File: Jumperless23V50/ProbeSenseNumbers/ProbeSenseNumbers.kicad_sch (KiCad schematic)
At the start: 117 parts, among them J1 Conn_01x05, J2 TopOutMAIN, J3 TopIn, J31 + - top, J32 + - bottom, J33 TopInMAIN, J34 TopOut, J35 BottomIn, J36 BottomOutMAIN, J4 BottomOut, J5 BottomInMAIN, J6 Conn_01x02

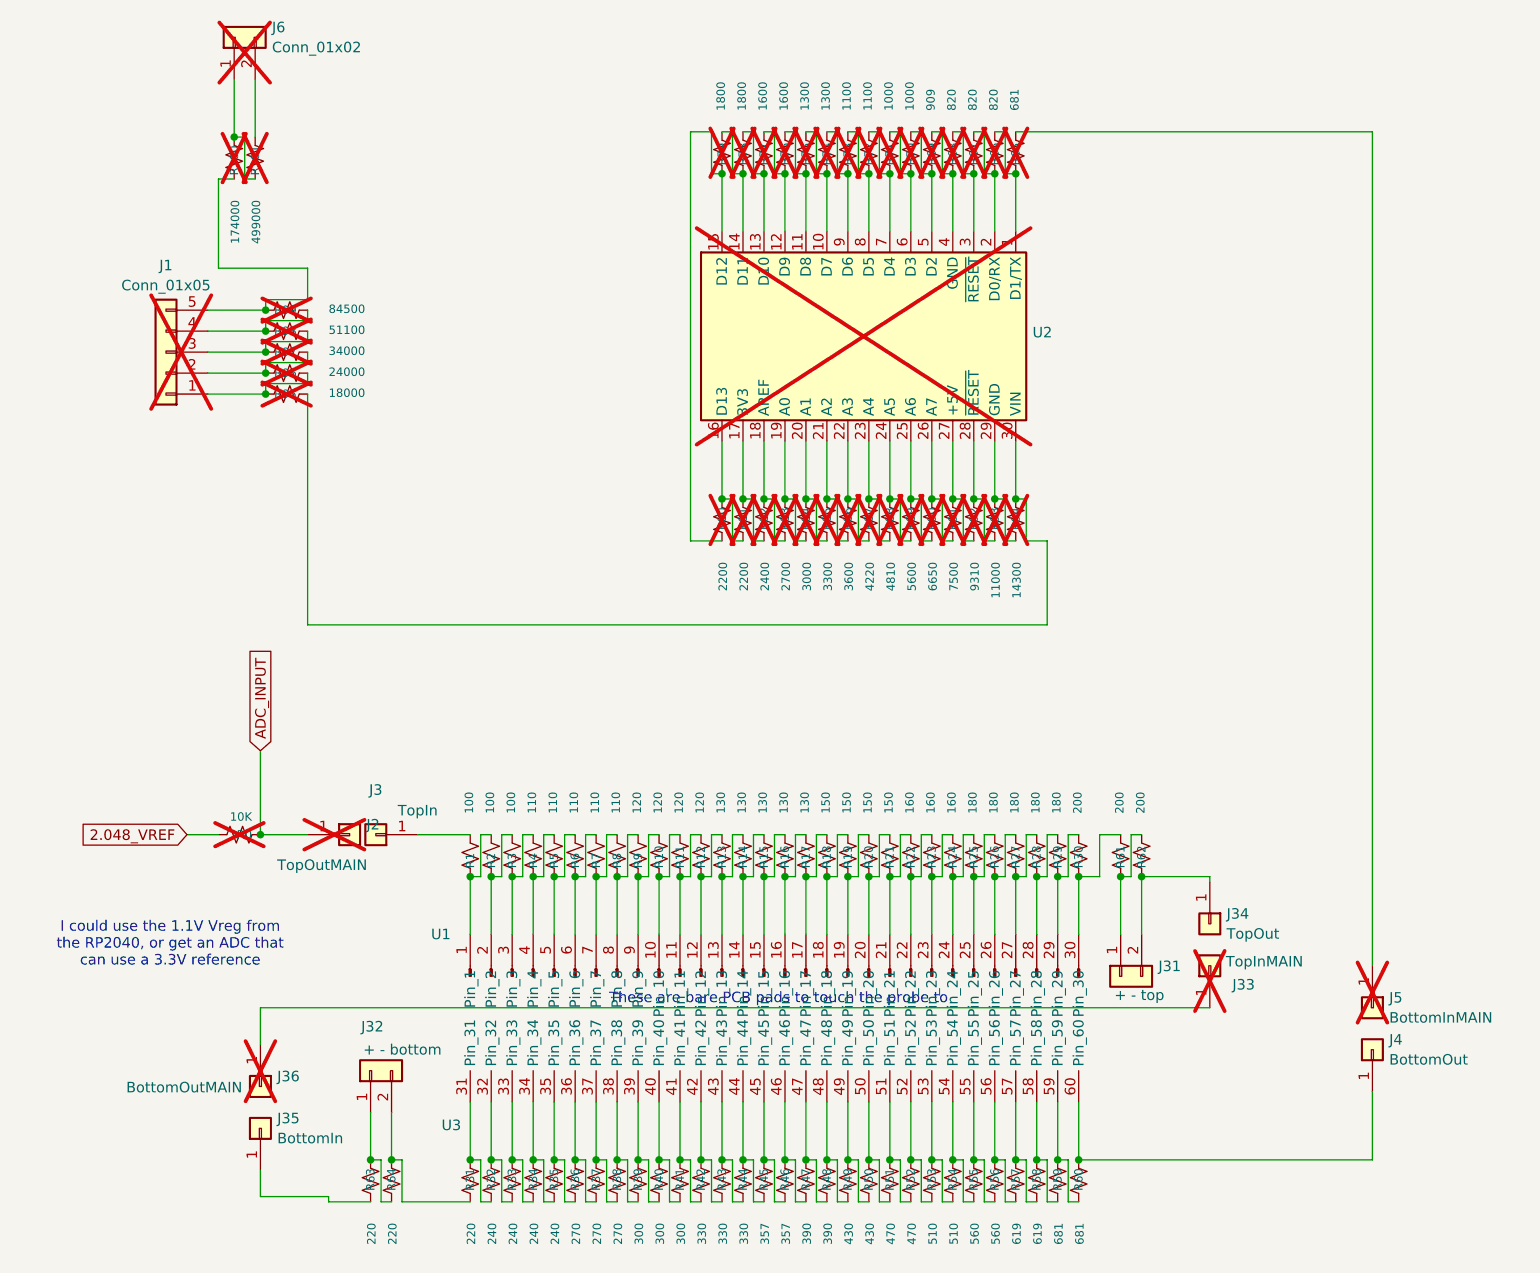
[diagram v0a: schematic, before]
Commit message: made a schematic with everything on one sheet
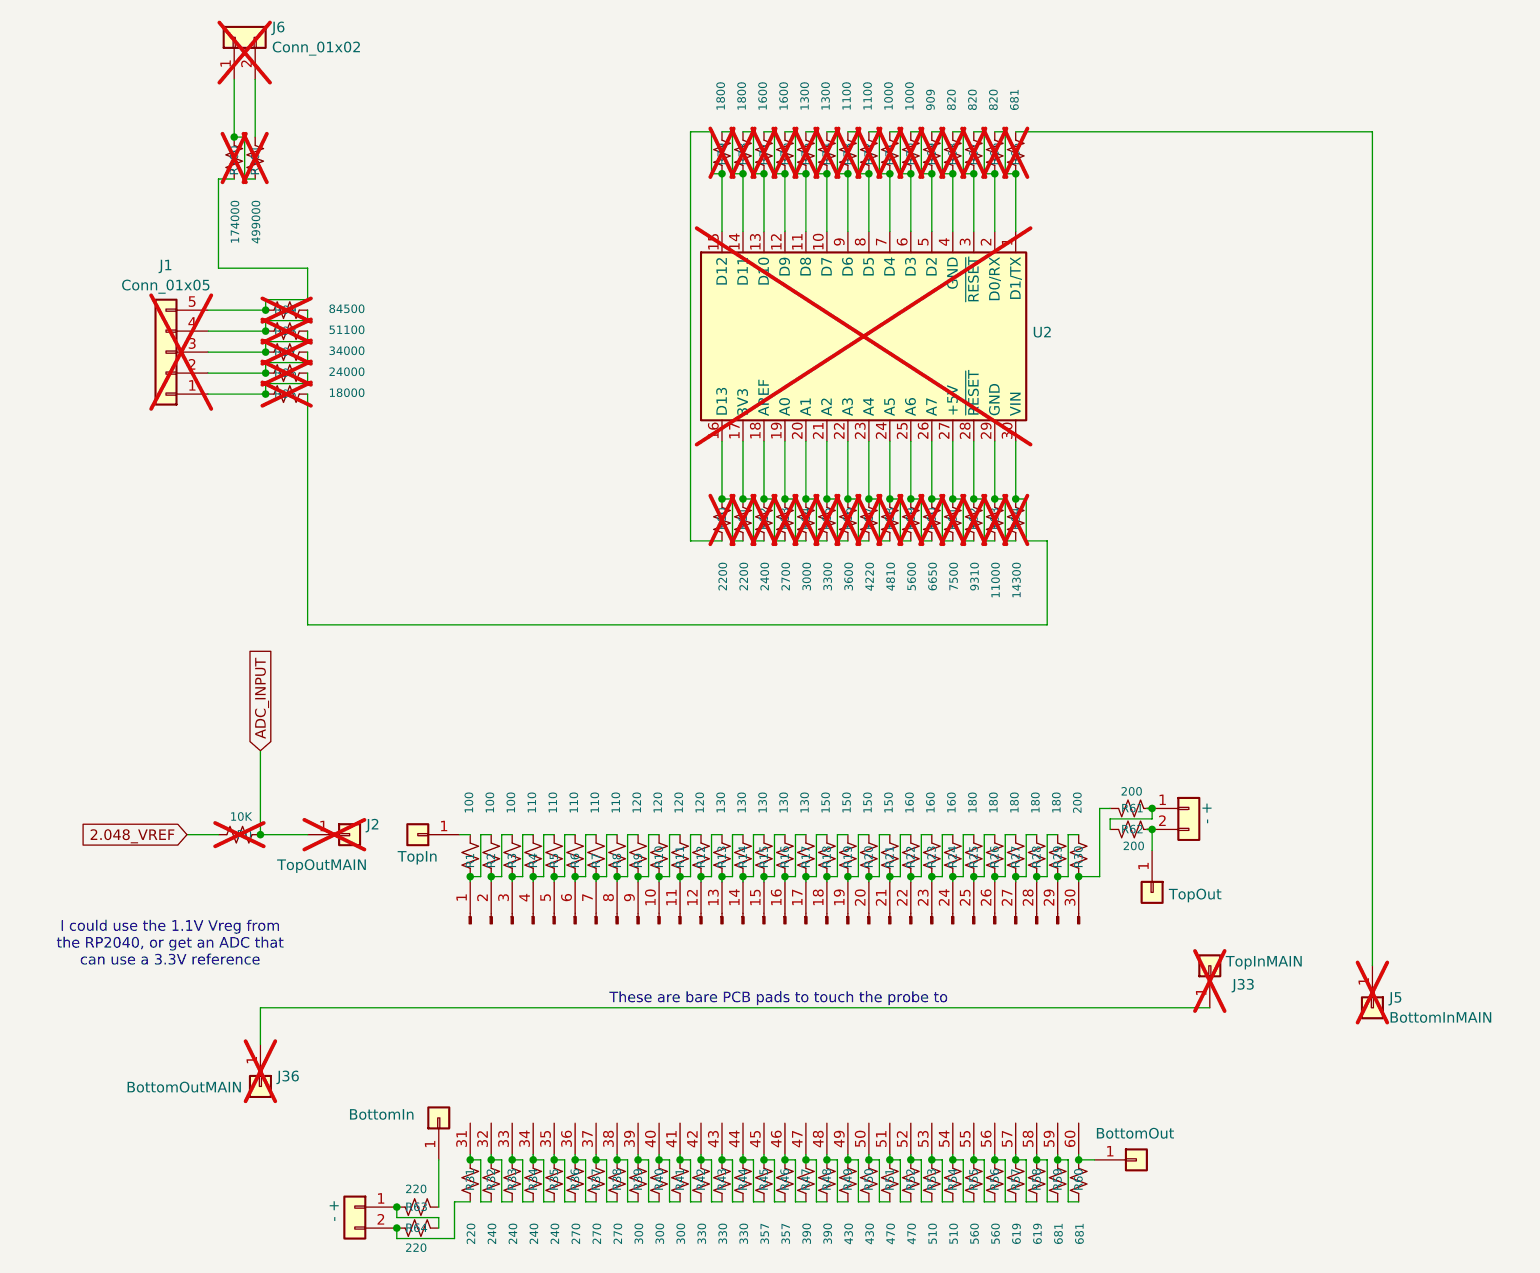
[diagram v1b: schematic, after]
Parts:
- J31: value + - top -> - +
- J32: value + - bottom -> - +
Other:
- moved on the sheet: R61, R62, R63, R64
